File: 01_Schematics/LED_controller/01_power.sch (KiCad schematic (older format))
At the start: 29 parts, among them J1 Pin, J2 Pin, J3 TB-03, J4 Pin, J49 Pin, J5 Pin, J6 Pin, J7 Pin, U1 MC34063AD, U2 UA78L12ACPK

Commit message: - Добавлена печатная плата; - Добавлены файлы посадочных мест использованных компонентов и STEP модели; - Добавлены файлы механической сборки (Solidworks);
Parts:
- removed D1: 1N5819, Diode_THT:D_DO-41_SOD81_P10.16mm_Horizontal, symbol Diode:1N5819
- added D1: B240, Diode_SMD:D_SMB, symbol Diode:B240
- added J50, J63, J64, J65, J66, J7-2: Pin, TestPoint:TestPoint_THTPad_2.0x2.0mm_Drill1.0mm, symbol Connector:Screw_Terminal_01x01
- added R12, R8: 0R, Resistor_SMD:R_0805_2012Metric_Pad1.15x1.40mm_HandSolder, symbol Device:R_Small
- F1: footprint Resistor_THT:R_Axial_DIN0204_L3.6mm_D1.6mm_P5.08mm_Horizontal -> extras:MF-R185
- J3: footprint TerminalBlock:TerminalBlock_bornier-3_P5.08mm -> extras:TB-03_metric
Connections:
- net +12V: now also J7-2.1 (Pin_1)
- net GNDD: now also D1.2 (A), R12.1
- net Vdrv: now also J66.1 (Pin_1), R8.2
- net Vin: now also J3.3 (Pin_3), J63.1 (Pin_1), R8.1; no longer J3.1 (Pin_1)
- net at L1.1, R5.1, U1.2 (SwE): now also D1.1 (K)
- net at R73.2: now also J3.1 (Pin_1), J50.1 (Pin_1), J64.1 (Pin_1), R12.2; no longer J3.3 (Pin_3)
- net at J3.2 (Pin_2), J49.1 (Pin_1): now also J65.1 (Pin_1)
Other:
- moved on the sheet: J1, J3
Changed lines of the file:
@@
 	1    0    0    -1
-$EndComp
-$Comp
-L Diode:1N5819 D1
-U 1 1 5BC4A972
-P 6300 2850
-F 0 "D1" H 6300 3066 50  0000 C CNN
-F 1 "1N5819" H 6300 2975 50  0000 C CNN
-F 2 "Diode_THT:D_DO-41_SOD81_P10.16mm_Horizontal" H 6300 2675 50  0001 C CNN
-F 3 "http://www.vishay.com/docs/88525/1n5817.pdf" H 6300 2850 50  0001 C CNN
-F 4 "1N5819" H 6300 2850 50  0001 C CNN "partnum"
-	1    6300 2850
-	0    1    1    0
 $EndComp
 Wire Wire Line
@@
 Wire Wire Line
 	4200 2300 4200 2200
-Text GLabel 2550 1650 0    50   Input ~ 0
+Text GLabel 2550 1550 0    50   Input ~ 0
 Vin
 $Comp
@@
 Wire Wire Line
 	3000 3100 3000 2850
-Text Label 2650 1650 0    50   ~ 0
+Text Label 2650 1550 0    50   ~ 0
 Vin
 Text Label 7450 2600 0    50   ~ 0
@@
 L Connector:Screw_Terminal_01x01 J1
 U 1 1 5C07DF1D
-P 2450 1800
-F 0 "J1" H 2530 1842 50  0000 L CNN
-F 1 "Pin" H 2530 1751 50  0000 L CNN
-F 2 "TestPoint:TestPoint_THTPad_2.0x2.0mm_Drill1.0mm" H 2450 1800 50  0001 C CNN
-F 3 "~" H 2450 1800 50  0001 C CNN
-	1    2450 1800
+P 2450 1700
+F 0 "J1" H 2530 1742 50  0000 L CNN
+F 1 "Pin" H 2530 1651 50  0000 L CNN
+F 2 "TestPoint:TestPoint_THTPad_2.0x2.0mm_Drill1.0mm" H 2450 1700 50  0001 C CNN
+F 3 "~" H 2450 1700 50  0001 C CNN
+	1    2450 1700
 	-1   0    0    1
 $EndComp
@@
 F 0 "F1" V 3247 2200 50  0000 C CNN
 F 1 "Fuse" V 3156 2200 50  0000 C CNN
-F 2 "Resistor_THT:R_Axial_DIN0204_L3.6mm_D1.6mm_P5.08mm_Horizontal" V 2980 2200 50  0001 C CNN
+F 2 "extras:MF-R185" V 2980 2200 50  0001 C CNN
 F 3 "~" H 3050 2200 50  0001 C CNN
 F 4 "MF-R090" V 3050 2200 50  0001 C CNN "partnum"
@@
 Connection ~ 3300 2200
 Wire Wire Line
-	2800 2200 2800 1800
-Wire Wire Line
-	2550 1650 2800 1650
-Connection ~ 2800 2200
-Wire Wire Line
-	2800 2200 2900 2200
-Wire Wire Line
-	2650 1800 2800 1800
-Connection ~ 2800 1800
-Wire Wire Line
-	2800 1800 2800 1650
+	2550 1550 2800 1550
+Wire Wire Line
+	2650 1700 2800 1700
+Connection ~ 2800 1700
+Wire Wire Line
+	2800 1700 2800 1550
 $Comp
 L Connector:Screw_Terminal_01x01 J2
@@
 $EndComp
 Wire Wire Line
-	7250 1800 7650 1800
+	7250 1800 7500 1800
 Text Label 7350 1800 0    50   ~ 0
 Vin
@@
 L Connector:Screw_Terminal_01x03 J?
 U 1 1 5C1457E9
-P 2350 2300
+P 2000 2300
 AR Path="/5BC5F278/5C1457E9" Ref="J?"  Part="1"
 AR Path="/5BC4A73F/5C1457E9" Ref="J3"  Part="1"
-F 0 "J3" H 2270 2617 50  0000 C CNN
-F 1 "TB-03" H 2270 2526 50  0000 C CNN
-F 2 "TerminalBlock:TerminalBlock_bornier-3_P5.08mm" H 2350 2300 50  0001 C CNN
-F 3 "~" H 2350 2300 50  0001 C CNN
-F 4 "TB-03" H 2350 2300 50  0001 C CNN "partnum"
-	1    2350 2300
-	-1   0    0    -1
+F 0 "J3" H 1920 2617 50  0000 C CNN
+F 1 "TB-03" H 1920 2526 50  0000 C CNN
+F 2 "extras:TB-03_metric" H 2000 2300 50  0001 C CNN
+F 3 "~" H 2000 2300 50  0001 C CNN
+F 4 "TB-03" H 2000 2300 50  0001 C CNN "partnum"
+	1    2000 2300
+	-1   0    0    1
 $EndComp
 Wire Wire Line
 	2750 2700 2750 2750
-Wire Wire Line
-	2550 2400 2750 2400
-Wire Wire Line
-	2550 2200 2800 2200
 $Comp
 L Connector:Screw_Terminal_01x01 J49
@@
 $EndComp
 Wire Wire Line
-	2850 2550 2850 2300
-Wire Wire Line
-	2850 2300 2550 2300
+	2850 2550 2850 2400
+$Comp
+L Connector:Screw_Terminal_01x01 J50
+U 1 1 5C361FAC
+P 2000 2750
+F 0 "J50" H 2080 2792 50  0000 L CNN
+F 1 "Pin" H 2080 2701 50  0000 L CNN
+F 2 "TestPoint:TestPoint_THTPad_2.0x2.0mm_Drill1.0mm" H 2000 2750 50  0001 C CNN
+F 3 "~" H 2000 2750 50  0001 C CNN
+	1    2000 2750
+	-1   0    0    1
+$EndComp
+Wire Wire Line
+	2200 2750 2250 2750
+Wire Wire Line
+	2250 2750 2250 2400
+Wire Wire Line
+	2800 1700 2800 1850
+Connection ~ 2800 2200
+Wire Wire Line
+	2800 2200 2900 2200
+$Comp
+L Connector:Screw_Terminal_01x01 J63
+U 1 1 5C6D49C8
+P 2450 1850
+F 0 "J63" H 2530 1892 50  0000 L CNN
+F 1 "Pin" H 2530 1801 50  0000 L CNN
+F 2 "TestPoint:TestPoint_THTPad_2.0x2.0mm_Drill1.0mm" H 2450 1850 50  0001 C CNN
+F 3 "~" H 2450 1850 50  0001 C CNN
+	1    2450 1850
+	-1   0    0    1
+$EndComp
+Wire Wire Line
+	2650 1850 2800 1850
+Connection ~ 2800 1850
+Wire Wire Line
+	2800 1850 2800 2200
+$Comp
+L Connector:Screw_Terminal_01x01 J64
+U 1 1 5C6D7C95
+P 2000 2900
+F 0 "J64" H 2080 2942 50  0000 L CNN
+F 1 "Pin" H 2080 2851 50  0000 L CNN
+F 2 "TestPoint:TestPoint_THTPad_2.0x2.0mm_Drill1.0mm" H 2000 2900 50  0001 C CNN
+F 3 "~" H 2000 2900 50  0001 C CNN
+	1    2000 2900
+	-1   0    0    1
+$EndComp
+Wire Wire Line
+	2200 2900 2250 2900
+Wire Wire Line
+	2250 2900 2250 2750
+Connection ~ 2250 2750
+$Comp
+L Connector:Screw_Terminal_01x01 J65
+U 1 1 5C6DE591
+P 3050 2400
+F 0 "J65" H 3130 2442 50  0000 L CNN
+F 1 "Pin" H 3130 2351 50  0000 L CNN
+F 2 "TestPoint:TestPoint_THTPad_2.0x2.0mm_Drill1.0mm" H 3050 2400 50  0001 C CNN
+F 3 "~" H 3050 2400 50  0001 C CNN
+	1    3050 2400
+	1    0    0    -1
+$EndComp
+Connection ~ 2850 2400
+Wire Wire Line
+	2850 2400 2850 2300
+$Comp
+L Connector:Screw_Terminal_01x01 J66
+U 1 1 5C6EC81E
+P 8250 1950
+F 0 "J66" H 8330 1992 50  0000 L CNN
+F 1 "Pin" H 8330 1901 50  0000 L CNN
+F 2 "TestPoint:TestPoint_THTPad_2.0x2.0mm_Drill1.0mm" H 8250 1950 50  0001 C CNN
+F 3 "~" H 8250 1950 50  0001 C CNN
+	1    8250 1950
+	1    0    0    -1
+$EndComp
+Wire Wire Line
+	8050 1950 7950 1950
+Wire Wire Line
+	7950 1950 7950 1800
+Wire Wire Line
+	2200 2400 2250 2400
+Wire Wire Line
+	2200 2300 2850 2300
+Wire Wire Line
+	2200 2200 2800 2200
+$Comp
+L Diode:B240 D?
+U 1 1 5C49EDA2
+P 6300 2850
+AR Path="/5C49EDA2" Ref="D?"  Part="1"
+AR Path="/5C0A300C/5C49EDA2" Ref="D?"  Part="1"
+AR Path="/5BC4A73F/5C49EDA2" Ref="D1"  Part="1"
+F 0 "D1" H 6300 3066 50  0000 C CNN
+F 1 "B240" H 6300 2975 50  0000 C CNN
+F 2 "Diode_SMD:D_SMB" H 6300 2675 50  0001 C CNN
+F 3 "http://www.jameco.com/Jameco/Products/ProdDS/1538777.pdf" H 6300 2850 50  0001 C CNN
+	1    6300 2850
+	0    1    1    0
+$EndComp
+Connection ~ 2250 2400
+Wire Wire Line
+	2250 2400 2500 2400
+$Comp
+L power:GNDD #PWR030
+U 1 1 5C4AEBA5
+P 2500 2750
+F 0 "#PWR030" H 2500 2500 50  0001 C CNN
+F 1 "GNDD" H 2504 2595 50  0000 C CNN
+F 2 "" H 2500 2750 50  0001 C CNN
+F 3 "" H 2500 2750 50  0001 C CNN
+	1    2500 2750
+	1    0    0    -1
+$EndComp
+$Comp
+L Device:R_Small R12
+U 1 1 5C4AEBAC
+P 2500 2600
+F 0 "R12" V 2696 2600 50  0000 C CNN
+F 1 "0R" V 2605 2600 50  0000 C CNN
+F 2 "Resistor_SMD:R_0805_2012Metric_Pad1.15x1.40mm_HandSolder" H 2500 2600 50  0001 C CNN
+F 3 "~" H 2500 2600 50  0001 C CNN
+F 4 "RC2010JK-070RL" V 2500 2600 50  0001 C CNN "partnum"
+	1    2500 2600
+	-1   0    0    1
+$EndComp
+Wire Wire Line
+	2500 2400 2500 2500
+Wire Wire Line
+	2500 2700 2500 2750
+Connection ~ 2500 2400
+Wire Wire Line
+	2500 2400 2750 2400
+$Comp
+L Device:R_Small R8
+U 1 1 5C4B27D6
+P 7750 1950
+F 0 "R8" V 7946 1950 50  0000 C CNN
+F 1 "0R" V 7855 1950 50  0000 C CNN
+F 2 "Resistor_SMD:R_0805_2012Metric_Pad1.15x1.40mm_HandSolder" H 7750 1950 50  0001 C CNN
+F 3 "~" H 7750 1950 50  0001 C CNN
+F 4 "RC2010JK-070RL" V 7750 1950 50  0001 C CNN "partnum"
+	1    7750 1950
+	0    -1   -1   0
+$EndComp
+Wire Wire Line
+	7950 1950 7850 1950
+Wire Wire Line
+	7650 1950 7500 1950
+Wire Wire Line
+	7500 1950 7500 1800
+Connection ~ 7500 1800
+Wire Wire Line
+	7500 1800 7650 1800
+Connection ~ 7950 1950
+$Comp
+L Connector:Screw_Terminal_01x01 J7-2
+U 1 1 5C656B95
+P 6250 4550
+F 0 "J7-2" H 6330 4592 50  0000 L CNN
+F 1 "Pin" H 6330 4501 50  0000 L CNN
+F 2 "TestPoint:TestPoint_THTPad_2.0x2.0mm_Drill1.0mm" H 6250 4550 50  0001 C CNN
+F 3 "~" H 6250 4550 50  0001 C CNN
+	1    6250 4550
+	1    0    0    -1
+$EndComp
+Wire Wire Line
+	6050 4550 5900 4550
+Wire Wire Line
+	5900 4550 5900 4350
+Connection ~ 5900 4350
 $EndSCHEMATC

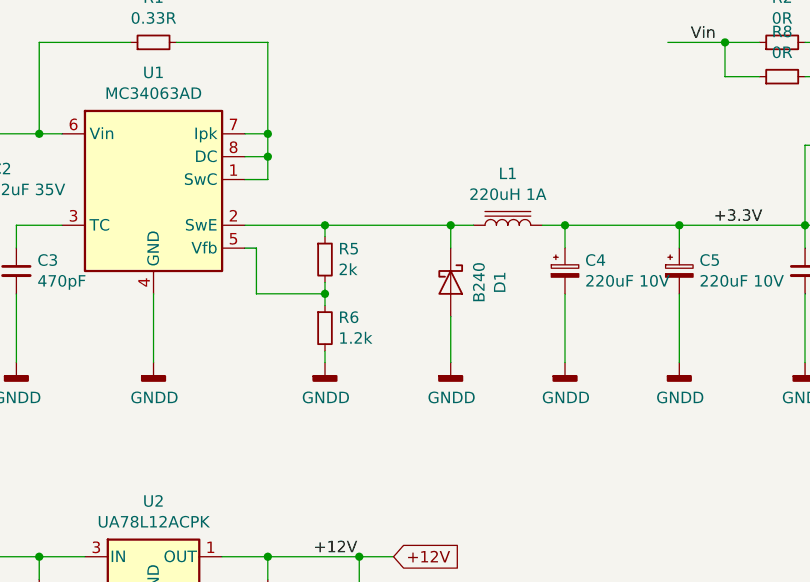
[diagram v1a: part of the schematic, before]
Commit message: - Исправлена ошибка с неправильным подключением цепи обратной связи микросхемы U1; - Плата переразведена с учетом изменений в схеме; - Добавлен файл BOM;
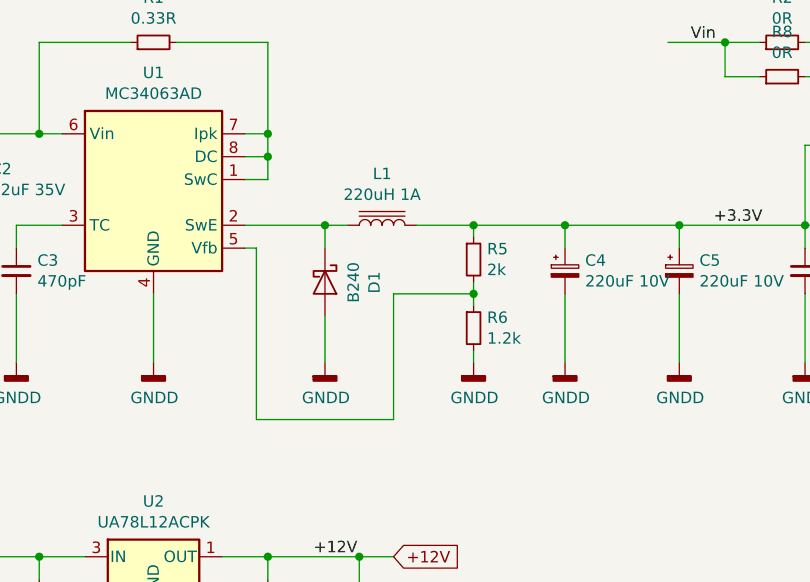
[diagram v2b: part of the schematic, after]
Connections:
- net +3.3V: now also R5.1
- net at D1.1 (K), L1.1, U1.2 (SwE): no longer R5.1
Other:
- moved on the sheet: D1, L1, R5, R6
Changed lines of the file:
@@
 $EndComp
 Wire Wire Line
-	5400 2600 5750 2600
-Wire Wire Line
-	6300 2600 6300 2700
+	5750 2600 5750 2700
 Wire Wire Line
 	5400 2200 5500 2200
@@
 L Device:L_Core_Iron L1
 U 1 1 5BC4AB9C
-P 6550 2600
-F 0 "L1" V 6775 2600 50  0000 C CNN
-F 1 "220uH 1A" V 6684 2600 50  0000 C CNN
-F 2 "extras:SRR1208" H 6550 2600 50  0001 C CNN
-F 3 "~" H 6550 2600 50  0001 C CNN
-F 4 "SRR1208-221KL" V 6550 2600 50  0001 C CNN "partnum"
-	1    6550 2600
+P 6000 2600
+F 0 "L1" V 6225 2600 50  0000 C CNN
+F 1 "220uH 1A" V 6134 2600 50  0000 C CNN
+F 2 "extras:SRR1208" H 6000 2600 50  0001 C CNN
+F 3 "~" H 6000 2600 50  0001 C CNN
+F 4 "SRR1208-221KL" V 6000 2600 50  0001 C CNN "partnum"
+	1    6000 2600
 	0    -1   -1   0
 $EndComp
 Wire Wire Line
-	6300 2600 6400 2600
-Connection ~ 6300 2600
+	5750 2600 5850 2600
 $Comp
 L Device:CP_Small C4
@@
 	1    0    0    -1
 $EndComp
-Wire Wire Line
-	6700 2600 6800 2600
 $Comp
 L power:GNDD #PWR08
 U 1 1 5BC4B117
-P 6300 3200
-F 0 "#PWR08" H 6300 2950 50  0001 C CNN
-F 1 "GNDD" H 6304 3045 50  0000 C CNN
-F 2 "" H 6300 3200 50  0001 C CNN
-F 3 "" H 6300 3200 50  0001 C CNN
-	1    6300 3200
+P 5750 3200
+F 0 "#PWR08" H 5750 2950 50  0001 C CNN
+F 1 "GNDD" H 5754 3045 50  0000 C CNN
+F 2 "" H 5750 3200 50  0001 C CNN
+F 3 "" H 5750 3200 50  0001 C CNN
+	1    5750 3200
 	1    0    0    -1
 $EndComp
@@
 L Device:R_Small R5
 U 1 1 5BC4C84A
-P 5750 2750
-F 0 "R5" H 5809 2796 50  0000 L CNN
-F 1 "2k" H 5809 2705 50  0000 L CNN
-F 2 "Resistor_SMD:R_0805_2012Metric_Pad1.15x1.40mm_HandSolder" H 5750 2750 50  0001 C CNN
-F 3 "~" H 5750 2750 50  0001 C CNN
-F 4 "RC0805FR-072KL" H 5750 2750 50  0001 C CNN "partnum"
-	1    5750 2750
+P 6400 2750
+F 0 "R5" H 6459 2796 50  0000 L CNN
+F 1 "2k" H 6459 2705 50  0000 L CNN
+F 2 "Resistor_SMD:R_0805_2012Metric_Pad1.15x1.40mm_HandSolder" H 6400 2750 50  0001 C CNN
+F 3 "~" H 6400 2750 50  0001 C CNN
+F 4 "RC0805FR-072KL" H 6400 2750 50  0001 C CNN "partnum"
+	1    6400 2750
 	1    0    0    -1
 $EndComp
@@
 L Device:R_Small R6
 U 1 1 5BC4CB89
-P 5750 3050
-F 0 "R6" H 5809 3096 50  0000 L CNN
-F 1 "1.2k" H 5809 3005 50  0000 L CNN
-F 2 "Resistor_SMD:R_0805_2012Metric_Pad1.15x1.40mm_HandSolder" H 5750 3050 50  0001 C CNN
-F 3 "~" H 5750 3050 50  0001 C CNN
-F 4 "RC0805FR-071K2L" H 5750 3050 50  0001 C CNN "partnum"
-	1    5750 3050
-	1    0    0    -1
-$EndComp
-Wire Wire Line
-	6300 3000 6300 3200
+P 6400 3050
+F 0 "R6" H 6459 3096 50  0000 L CNN
+F 1 "1.2k" H 6459 3005 50  0000 L CNN
+F 2 "Resistor_SMD:R_0805_2012Metric_Pad1.15x1.40mm_HandSolder" H 6400 3050 50  0001 C CNN
+F 3 "~" H 6400 3050 50  0001 C CNN
+F 4 "RC0805FR-071K2L" H 6400 3050 50  0001 C CNN "partnum"
+	1    6400 3050
+	1    0    0    -1
+$EndComp
+Wire Wire Line
+	5750 3000 5750 3200
 Wire Wire Line
 	6800 2900 6800 3200
@@
 L power:GNDD #PWR07
 U 1 1 5BC4D3B2
-P 5750 3200
-F 0 "#PWR07" H 5750 2950 50  0001 C CNN
-F 1 "GNDD" H 5754 3045 50  0000 C CNN
-F 2 "" H 5750 3200 50  0001 C CNN
-F 3 "" H 5750 3200 50  0001 C CNN
-	1    5750 3200
-	1    0    0    -1
-$EndComp
-Wire Wire Line
-	5750 3150 5750 3200
-Wire Wire Line
-	5750 2850 5750 2900
-Wire Wire Line
-	5750 2650 5750 2600
-Connection ~ 5750 2600
-Wire Wire Line
-	5750 2600 6300 2600
-Wire Wire Line
-	5450 2900 5450 2700
-Connection ~ 5750 2900
-Wire Wire Line
-	5750 2900 5750 2950
+P 6400 3200
+F 0 "#PWR07" H 6400 2950 50  0001 C CNN
+F 1 "GNDD" H 6404 3045 50  0000 C CNN
+F 2 "" H 6400 3200 50  0001 C CNN
+F 3 "" H 6400 3200 50  0001 C CNN
+	1    6400 3200
+	1    0    0    -1
+$EndComp
+Wire Wire Line
+	6400 3150 6400 3200
 Wire Wire Line
 	5450 2700 5400 2700
-Wire Wire Line
-	5450 2900 5750 2900
 $Comp
 L Device:R_Small R1
@@
 L Diode:B240 D?
 U 1 1 5C49EDA2
-P 6300 2850
+P 5750 2850
 AR Path="/5C49EDA2" Ref="D?"  Part="1"
 AR Path="/5C0A300C/5C49EDA2" Ref="D?"  Part="1"
 AR Path="/5BC4A73F/5C49EDA2" Ref="D1"  Part="1"
-F 0 "D1" H 6300 3066 50  0000 C CNN
-F 1 "B240" H 6300 2975 50  0000 C CNN
-F 2 "Diode_SMD:D_SMB" H 6300 2675 50  0001 C CNN
-F 3 "http://www.jameco.com/Jameco/Products/ProdDS/1538777.pdf" H 6300 2850 50  0001 C CNN
-	1    6300 2850
+F 0 "D1" H 5750 3066 50  0000 C CNN
+F 1 "B240" H 5750 2975 50  0000 C CNN
+F 2 "Diode_SMD:D_SMB" H 5750 2675 50  0001 C CNN
+F 3 "http://www.jameco.com/Jameco/Products/ProdDS/1538777.pdf" H 5750 2850 50  0001 C CNN
+	1    5750 2850
 	0    1    1    0
 $EndComp
@@
 	5900 4550 5900 4350
 Connection ~ 5900 4350
+Wire Wire Line
+	6400 2850 6400 2900
+Wire Wire Line
+	5750 2600 5400 2600
+Connection ~ 5750 2600
+Wire Wire Line
+	6150 2600 6400 2600
+Wire Wire Line
+	6400 2650 6400 2600
+Connection ~ 6400 2600
+Wire Wire Line
+	6400 2600 6800 2600
+Wire Wire Line
+	6400 2900 6050 2900
+Wire Wire Line
+	6050 3450 5450 3450
+Connection ~ 6400 2900
+Wire Wire Line
+	6400 2900 6400 2950
+Wire Wire Line
+	5450 2700 5450 3450
+Wire Wire Line
+	6050 2900 6050 3450
 $EndSCHEMATC
